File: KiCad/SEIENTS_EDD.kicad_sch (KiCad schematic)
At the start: 0 parts

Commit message: Cambio
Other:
- added sheet ALIMENTACIO (ALIMENTACIO.kicad_sch)
- added sheet DRIVERS(MOTORS) (DRIVERS(MOTORS).kicad_sch)
- added sheet MICROCONTROLADOR (MICROCONTROLADOR.kicad_sch)
- added sheet SENSORS (SENSORS.kicad_sch)
- note added: "ALIMENTACIO"
- note added: "MICROCONTROLADOR"
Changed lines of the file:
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@@
 	(generator_version "9.0")
 	(paper "A4")
+	(text "ALIMENTACIO"
+		(exclude_from_sim no)
+		(at 62.738 62.484 0)
+		(effects
+			(font
+				(size 5.08 5.08)
+			)
+		)
+	)
+	(text "MICROCONTROLADOR\n"
+		(exclude_from_sim no)
+		(at 131.064 63.246 0)
+		(effects
+			(font
+				(size 3.81 3.81)
+			)
+		)
+	)
+	(sheet
+		(at 99.06 27.94)
+		(size 63.5 71.12)
+		(exclude_from_sim no)
+		(in_bom yes)
+		(on_board yes)
+		(dnp no)
+		(fields_autoplaced yes)
+		(stroke
+			(width 0.1524)
+			(type solid)
+		)
+		(fill
+			(color 0 0 0 0.0000)
+		)
+		(property "Sheetname" "MICROCONTROLADOR"
+			(at 99.06 27.2284 0)
+			(effects
+				(font
+					(size 1.27 1.27)
+				)
+				(justify left bottom)
+			)
+		)
+		(property "Sheetfile" "MICROCONTROLADOR.kicad_sch"
+			(at 99.06 99.6446 0)
+			(effects
+				(font
+					(size 1.27 1.27)
+				)
+				(justify left top)
+			)
+		)
+		(instances
+			(project "SEIENTS_EDD"
+				(path "/b6401b4f-5426-49b8-bb2e-8ecdb19989ef"
+					(page "3")
+				)
+			)
+		)
+	)
+	(sheet
+		(at 31.75 27.94)
+		(size 62.23 71.12)
+		(exclude_from_sim no)
+		(in_bom yes)
+		(on_board yes)
+		(dnp no)
+		(fields_autoplaced yes)
+		(stroke
+			(width 0.1524)
+			(type solid)
+		)
+		(fill
+			(color 0 0 0 0.0000)
+		)
+		(property "Sheetname" "ALIMENTACIO"
+			(at 31.75 27.2284 0)
+			(effects
+				(font
+					(size 1.27 1.27)
+				)
+				(justify left bottom)
+			)
+		)
+		(property "Sheetfile" "ALIMENTACIO.kicad_sch"
+			(at 31.75 99.6446 0)
+			(effects
+				(font
+					(size 1.27 1.27)
+				)
+				(justify left top)
+			)
+		)
+		(instances
+			(project "SEIENTS_EDD"
+				(path "/b6401b4f-5426-49b8-bb2e-8ecdb19989ef"
+					(page "2")
+				)
+			)
+		)
+	)
+	(sheet
+		(at 34.29 113.03)
+		(size 59.69 54.61)
+		(exclude_from_sim no)
+		(in_bom yes)
+		(on_board yes)
+		(dnp no)
+		(fields_autoplaced yes)
+		(stroke
+			(width 0.1524)
+			(type solid)
+		)
+		(fill
+			(color 0 0 0 0.0000)
+		)
+		(property "Sheetname" "DRIVERS(MOTORS)"
+			(at 34.29 112.3184 0)
+			(effects
+				(font
+					(size 1.27 1.27)
+				)
+				(justify left bottom)
+			)
+		)
+		(property "Sheetfile" "DRIVERS(MOTORS).kicad_sch"
+			(at 34.29 168.2246 0)
+			(effects
+				(font
+					(size 1.27 1.27)
+				)
+				(justify left top)
+			)
+		)
+		(instances
+			(project "SEIENTS_EDD"
+				(path "/b6401b4f-5426-49b8-bb2e-8ecdb19989ef"
+					(page "5")
+				)
+			)
+		)
+	)
+	(sheet
+		(at 168.91 29.21)
+		(size 77.47 69.85)
+		(exclude_from_sim no)
+		(in_bom yes)
+		(on_board yes)
+		(dnp no)
+		(fields_autoplaced yes)
+		(stroke
+			(width 0.1524)
+			(type solid)
+		)
+		(fill
+			(color 0 0 0 0.0000)
+		)
+		(property "Sheetname" "SENSORS"
+			(at 168.91 28.4984 0)
+			(effects
+				(font
+					(size 1.27 1.27)
+				)
+				(justify left bottom)
+			)
+		)
+		(property "Sheetfile" "SENSORS.kicad_sch"
+			(at 168.91 99.6446 0)
+			(effects
+				(font
+					(size 1.27 1.27)
+				)
+				(justify left top)
+			)
+		)
+		(instances
+			(project "SEIENTS_EDD"
+				(path "/b6401b4f-5426-49b8-bb2e-8ecdb19989ef"
+					(page "4")
+				)
+			)
+		)
+	)
 	(sheet_instances
 		(path "/"

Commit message: Noms blocs
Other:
- note added: "DRIVERS"
- note added: "SENSORS"
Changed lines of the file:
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@@
 	(generator_version "9.0")
 	(paper "A4")
+	(text "DRIVERS"
+		(exclude_from_sim no)
+		(at 62.23 139.446 0)
+		(effects
+			(font
+				(size 5.08 5.08)
+			)
+		)
+	)
+	(text "SENSORS"
+		(exclude_from_sim no)
+		(at 202.692 64.516 0)
+		(effects
+			(font
+				(size 5.08 5.08)
+			)
+		)
+	)
 	(text "ALIMENTACIO"
 		(exclude_from_sim no)
@@
 	)
 	(sheet
-		(at 34.29 113.03)
-		(size 59.69 54.61)
+		(at 31.75 110.49)
+		(size 62.23 59.69)
 		(exclude_from_sim no)
 		(in_bom yes)
@@
 		)
 		(property "Sheetname" "DRIVERS(MOTORS)"
-			(at 34.29 112.3184 0)
+			(at 31.75 109.7784 0)
 			(effects
 				(font
@@
 		)
 		(property "Sheetfile" "DRIVERS(MOTORS).kicad_sch"
-			(at 34.29 168.2246 0)
+			(at 31.75 170.7646 0)
 			(effects
 				(font
@@
 	(sheet
 		(at 168.91 29.21)
-		(size 77.47 69.85)
+		(size 67.31 69.85)
 		(exclude_from_sim no)
 		(in_bom yes)

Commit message: BOTONERA
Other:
- added sheet BOTONERA (BOTONERA.kicad_sch)
- note added: "BOTONERA"
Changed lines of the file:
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@@
+		)
+	)
+	(text "BOTONERA"
+		(exclude_from_sim no)
+		(at 129.794 139.7 0)
+		(effects
+			(font
+				(size 5.08 5.08)
+			)
 		)
 	)
@@
 				)
 			)
+		)
+	)
+	(sheet
+		(at 99.06 110.49)
+		(size 64.77 59.69)
+		(exclude_from_sim no)
+		(in_bom yes)
+		(on_board yes)
+		(dnp no)
+		(fields_autoplaced yes)
+		(stroke
+			(width 0.1524)
+			(type solid)
+		)
+		(fill
+			(color 0 0 0 0.0000)
+		)
+		(property "Sheetname" "BOTONERA"
+			(at 99.06 109.7784 0)
+			(effects
+				(font
+					(size 1.27 1.27)
+				)
+				(justify left bottom)
+			)
+		)
+		(property "Sheetfile" "BOTONERA.kicad_sch"
+			(at 99.06 170.7646 0)
+			(effects
+				(font
+					(size 1.27 1.27)
+				)
+				(justify left top)
+			)
+		)
+		(instances
+			(project "SEIENTS_EDD"
+				(path "/b6401b4f-5426-49b8-bb2e-8ecdb19989ef"
+					(page "6")
+				)
+			)

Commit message: Canvis a l'alimentació: part acabada
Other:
- note added: "ALIMENTACIÓ"
- note removed: "ALIMENTACIO"
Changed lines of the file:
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@@
 		)
 	)
-	(text "ALIMENTACIO"
+	(text "ALIMENTACIÓ"
 		(exclude_from_sim no)
 		(at 62.738 62.484 0)

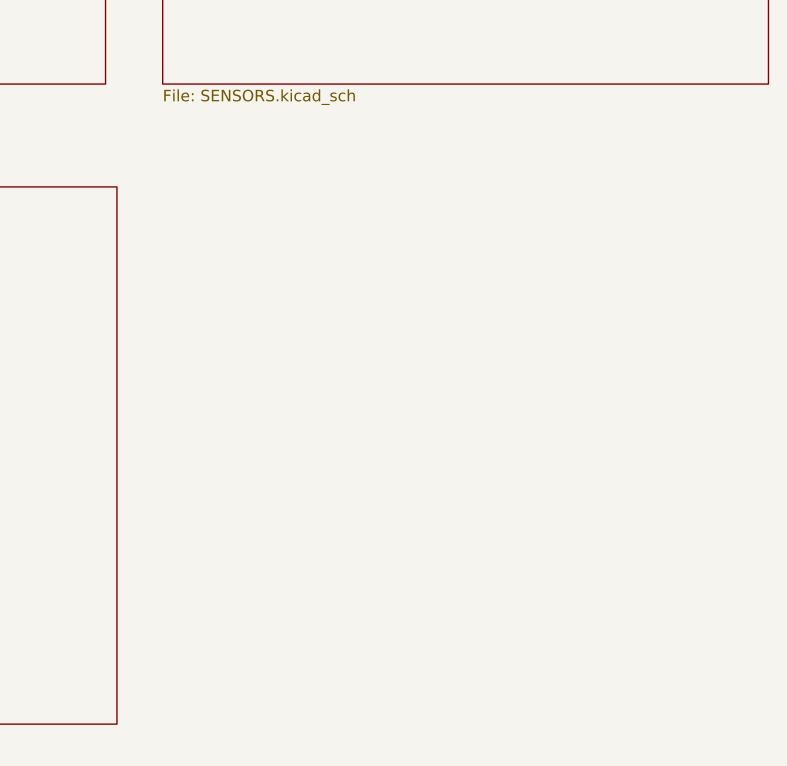
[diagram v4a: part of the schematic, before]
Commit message: Afegit CAN
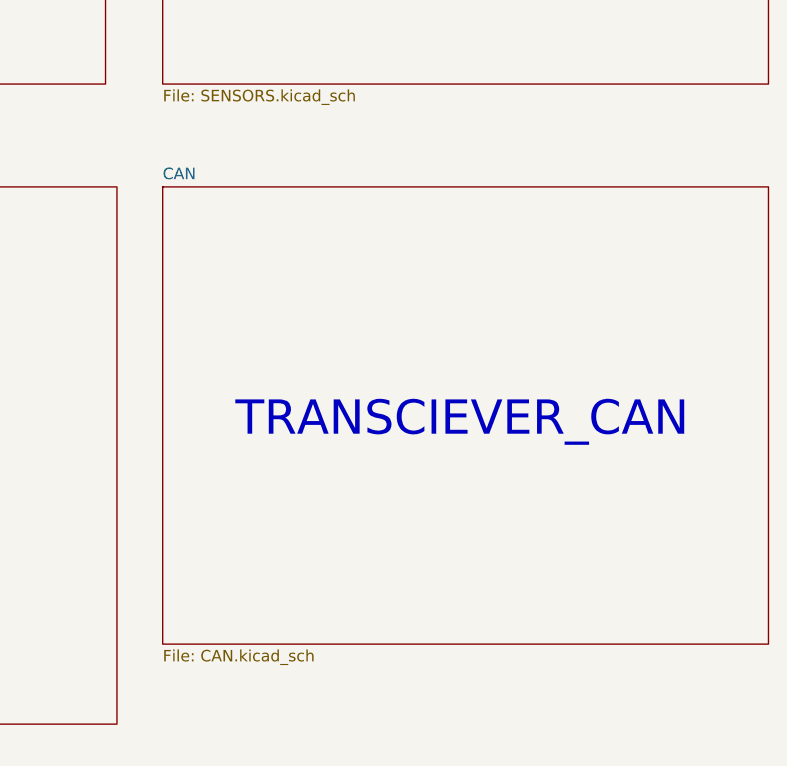
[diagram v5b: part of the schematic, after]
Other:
- added sheet CAN (CAN.kicad_sch)
- note added: "TRANSCIEVER_CAN"
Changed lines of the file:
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@@
 	(generator_version "9.0")
 	(paper "A4")
+	(text "TRANSCIEVER_CAN"
+		(exclude_from_sim no)
+		(at 202.184 136.398 0)
+		(effects
+			(font
+				(size 3.81 3.81)
+			)
+		)
+	)
 	(text "DRIVERS"
 		(exclude_from_sim no)
@@
 			)
 		)
+	)
+	(sheet
+		(at 168.91 110.49)
+		(size 67.31 50.8)
+		(exclude_from_sim no)
+		(in_bom yes)
+		(on_board yes)
+		(dnp no)
+		(fields_autoplaced yes)
+		(stroke
+			(width 0.1524)
+			(type solid)
+		)
+		(fill
+			(color 0 0 0 0.0000)
+		)
+		(property "Sheetname" "CAN"
+			(at 168.91 109.7784 0)
+			(effects
+				(font
+					(size 1.27 1.27)
+				)
+				(justify left bottom)
+			)
+		)
+		(property "Sheetfile" "CAN.kicad_sch"
+			(at 168.91 161.8746 0)
+			(effects
+				(font
+					(size 1.27 1.27)
+				)
+				(justify left top)
+			)
+		)
+		(instances
+			(project "SEIENTS_EDD"
+				(path "/b6401b4f-5426-49b8-bb2e-8ecdb19989ef"
+					(page "7")
+				)
+			)
+		)

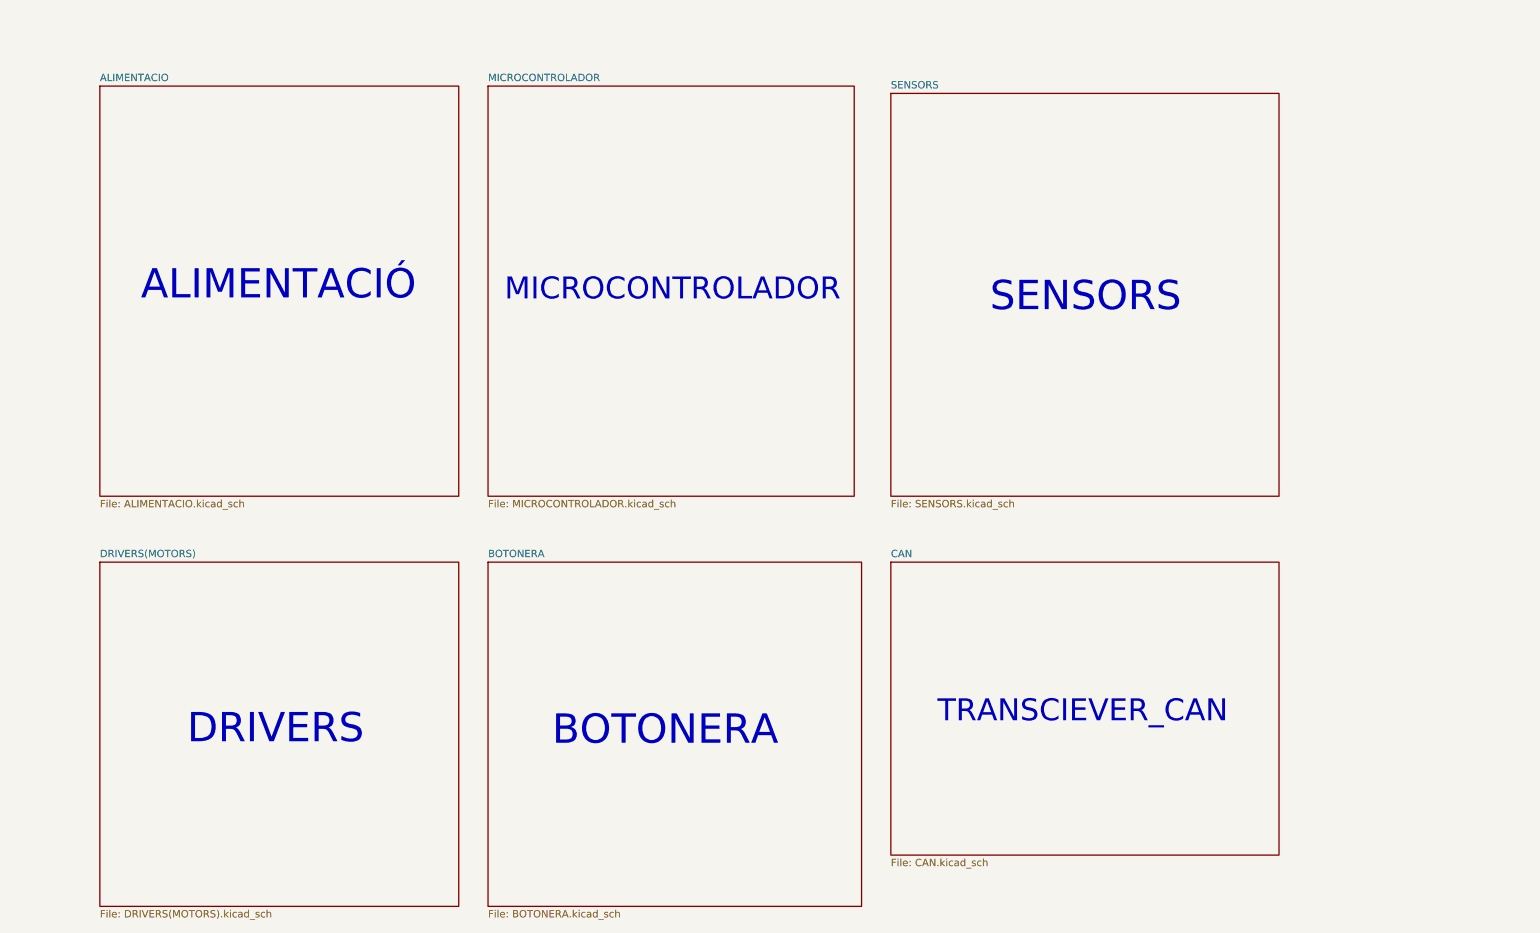
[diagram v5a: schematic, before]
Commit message: Afegist el MOSFET
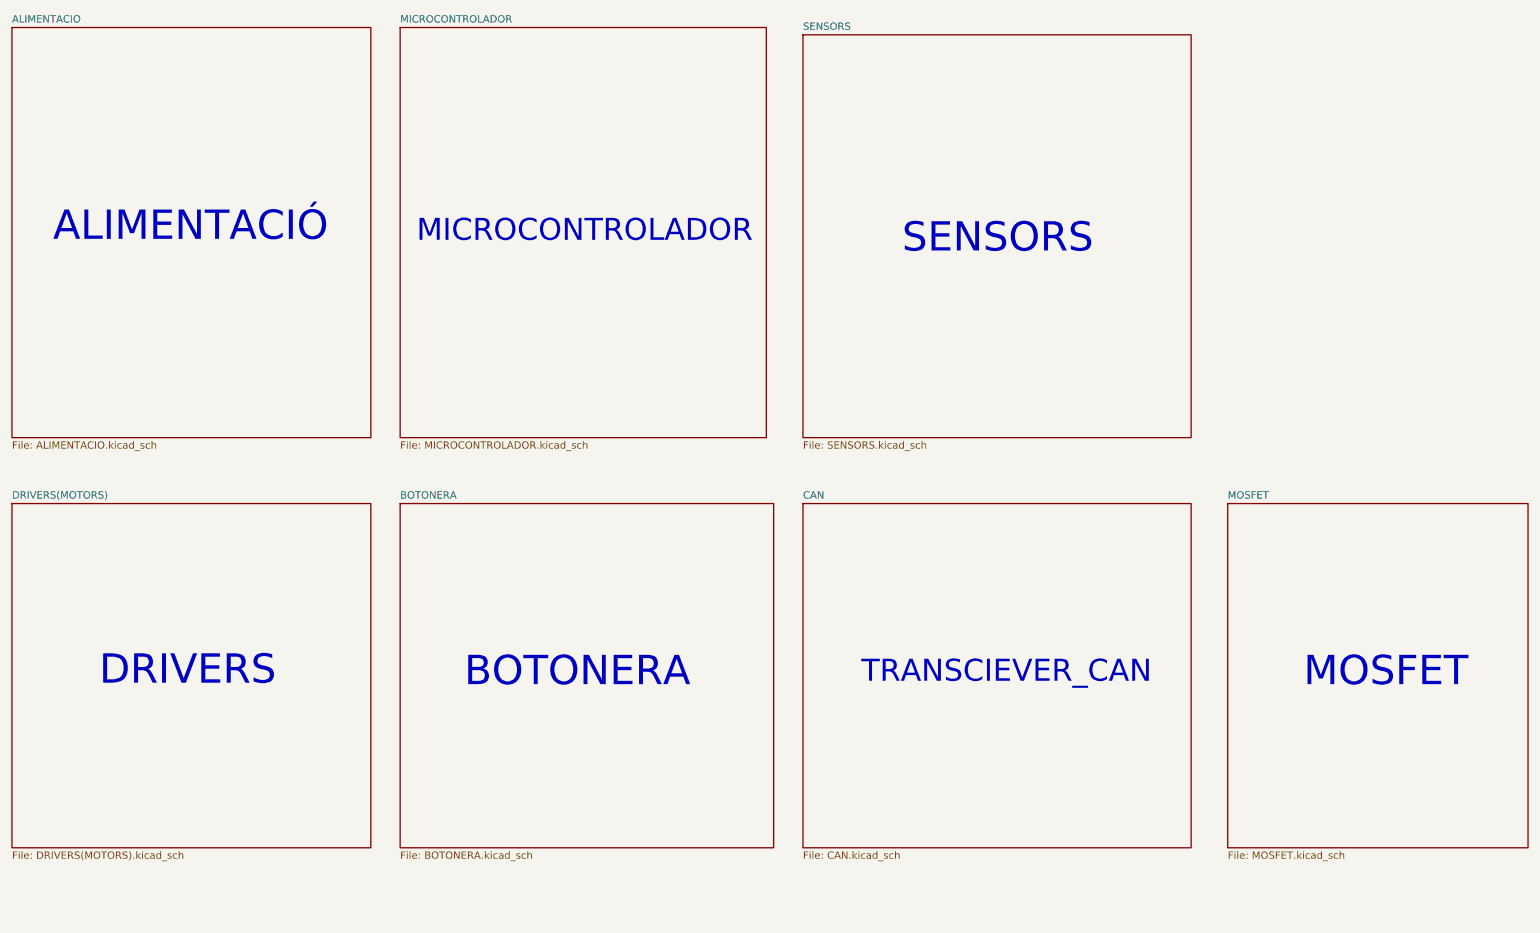
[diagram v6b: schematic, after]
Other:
- added sheet MOSFET (MOSFET.kicad_sch)
- note added: "MOSFET"
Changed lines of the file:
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@@
 	(text "TRANSCIEVER_CAN"
 		(exclude_from_sim no)
-		(at 202.184 136.398 0)
+		(at 188.976 129.54 0)
 		(effects
 			(font
@@
 	(text "DRIVERS"
 		(exclude_from_sim no)
-		(at 62.23 139.446 0)
+		(at 46.99 129.286 0)
 		(effects
 			(font
@@
 	(text "SENSORS"
 		(exclude_from_sim no)
-		(at 202.692 64.516 0)
+		(at 187.452 54.356 0)
 		(effects
 			(font
@@
 	(text "ALIMENTACIÓ"
 		(exclude_from_sim no)
-		(at 62.738 62.484 0)
+		(at 47.498 52.324 0)
 		(effects
 			(font
@@
 	(text "MICROCONTROLADOR\n"
 		(exclude_from_sim no)
-		(at 131.064 63.246 0)
+		(at 115.824 53.086 0)
 		(effects
 			(font
@@
 		)
 	)
+	(text "MOSFET\n"
+		(exclude_from_sim no)
+		(at 254.762 129.54 0)
+		(effects
+			(font
+				(size 5.08 5.08)
+			)
+		)
+	)
 	(text "BOTONERA"
 		(exclude_from_sim no)
-		(at 129.794 139.7 0)
-		(effects
-			(font
-				(size 5.08 5.08)
-			)
-		)
-	)
-	(sheet
-		(at 168.91 110.49)
-		(size 67.31 50.8)
+		(at 114.554 129.54 0)
+		(effects
+			(font
+				(size 5.08 5.08)
+			)
+		)
+	)
+	(sheet
+		(at 153.67 100.33)
+		(size 67.31 59.69)
 		(exclude_from_sim no)
 		(in_bom yes)
@@
 		)
 		(property "Sheetname" "CAN"
-			(at 168.91 109.7784 0)
+			(at 153.67 99.6184 0)
 			(effects
 				(font
@@
 		)
 		(property "Sheetfile" "CAN.kicad_sch"
-			(at 168.91 161.8746 0)
+			(at 153.67 160.6046 0)
 			(effects
 				(font
@@
 	)
 	(sheet
-		(at 99.06 27.94)
+		(at 83.82 17.78)
 		(size 63.5 71.12)
 		(exclude_from_sim no)
@@
 		)
 		(property "Sheetname" "MICROCONTROLADOR"
-			(at 99.06 27.2284 0)
+			(at 83.82 17.0684 0)
 			(effects
 				(font
@@
 		)
 		(property "Sheetfile" "MICROCONTROLADOR.kicad_sch"
-			(at 99.06 99.6446 0)
+			(at 83.82 89.4846 0)
 			(effects
 				(font
@@
 	)
 	(sheet
-		(at 31.75 27.94)
+		(at 16.51 17.78)
 		(size 62.23 71.12)
 		(exclude_from_sim no)
@@
 		)
 		(property "Sheetname" "ALIMENTACIO"
-			(at 31.75 27.2284 0)
+			(at 16.51 17.0684 0)
 			(effects
 				(font
@@
 		)
 		(property "Sheetfile" "ALIMENTACIO.kicad_sch"
-			(at 31.75 99.6446 0)
+			(at 16.51 89.4846 0)
 			(effects
 				(font
@@
 	)
 	(sheet
-		(at 31.75 110.49)
+		(at 16.51 100.33)
 		(size 62.23 59.69)
 		(exclude_from_sim no)
@@
 		)
 		(property "Sheetname" "DRIVERS(MOTORS)"
-			(at 31.75 109.7784 0)
+			(at 16.51 99.6184 0)
 			(effects
 				(font
@@
 		)
 		(property "Sheetfile" "DRIVERS(MOTORS).kicad_sch"
-			(at 31.75 170.7646 0)
+			(at 16.51 160.6046 0)
 			(effects
 				(font
@@
 	)
 	(sheet
-		(at 99.06 110.49)
+		(at 83.82 100.33)
 		(size 64.77 59.69)
 		(exclude_from_sim no)
@@
 		)
 		(property "Sheetname" "BOTONERA"
-			(at 99.06 109.7784 0)
+			(at 83.82 99.6184 0)
 			(effects
 				(font
@@
 		)
 		(property "Sheetfile" "BOTONERA.kicad_sch"
-			(at 99.06 170.7646 0)
+			(at 83.82 160.6046 0)
 			(effects
 				(font
@@
 	)
 	(sheet
-		(at 168.91 29.21)
+		(at 227.33 100.33)
+		(size 52.07 59.69)
+		(exclude_from_sim no)
+		(in_bom yes)
+		(on_board yes)
+		(dnp no)
+		(fields_autoplaced yes)
+		(stroke
+			(width 0.1524)
+			(type solid)
+		)
+		(fill
+			(color 0 0 0 0.0000)
+		)
+		(property "Sheetname" "MOSFET"
+			(at 227.33 99.6184 0)
+			(effects
+				(font
+					(size 1.27 1.27)
+				)
+				(justify left bottom)
+			)
+		)
+		(property "Sheetfile" "MOSFET.kicad_sch"
+			(at 227.33 160.6046 0)
+			(effects
+				(font
+					(size 1.27 1.27)
+				)
+				(justify left top)
+			)
+		)
+		(instances
+			(project "SEIENTS_EDD"
+				(path "/b6401b4f-5426-49b8-bb2e-8ecdb19989ef"
+					(page "8")
+				)
+			)
+		)
+	)
+	(sheet
+		(at 153.67 19.05)
 		(size 67.31 69.85)
 		(exclude_from_sim no)
@@
 		)
 		(property "Sheetname" "SENSORS"
-			(at 168.91 28.4984 0)
+			(at 153.67 18.3384 0)
 			(effects
 				(font
@@
 		)
 		(property "Sheetfile" "SENSORS.kicad_sch"
-			(at 168.91 99.6446 0)
-			(effects
-				(font
+			(at 153.67 89.4846 0)
+			(effects
+				(font

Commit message: Modificacio
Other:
- added sheet EEPROM (EEPROM.kicad_sch)
- note added: "EEPROM"
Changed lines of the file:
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@@
+		)
+	)
+	(text "EEPROM"
+		(exclude_from_sim no)
+		(at 254.254 54.102 0)
+		(effects
+			(font
+				(size 5.08 5.08)
+			)
 		)
 	)
@@
 				)
 			)
+		)
+	)
+	(sheet
+		(at 228.6 19.05)
+		(size 50.8 69.85)
+		(exclude_from_sim no)
+		(in_bom yes)
+		(on_board yes)
+		(dnp no)
+		(fields_autoplaced yes)
+		(stroke
+			(width 0.1524)
+			(type solid)
+		)
+		(fill
+			(color 0 0 0 0.0000)
+		)
+		(property "Sheetname" "EEPROM"
+			(at 228.6 18.3384 0)
+			(effects
+				(font
+					(size 1.27 1.27)
+				)
+				(justify left bottom)
+			)
+		)
+		(property "Sheetfile" "EEPROM.kicad_sch"
+			(at 228.6 89.4846 0)
+			(effects
+				(font
+					(size 1.27 1.27)
+				)
+				(justify left top)
+			)
+		)
+		(instances
+			(project "SEIENTS_EDD"
+				(path "/b6401b4f-5426-49b8-bb2e-8ecdb19989ef"
+					(page "9")
+				)
+			)
